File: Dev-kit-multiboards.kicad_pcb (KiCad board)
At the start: 2 copper layers, 93.9 x 100 mm, 27 parts, among them J1 Conn_01x04_Socket, J2 Conn_01x04_Socket, J3 Conn_01x02_Socket, J4 Conn_01x19_Socket, J5 Conn_01x19_Socket, J6 Conn_01x02_Socket, J7 Conn_01x02_Socket, J8 Conn_02x17_Counter_Clockwise

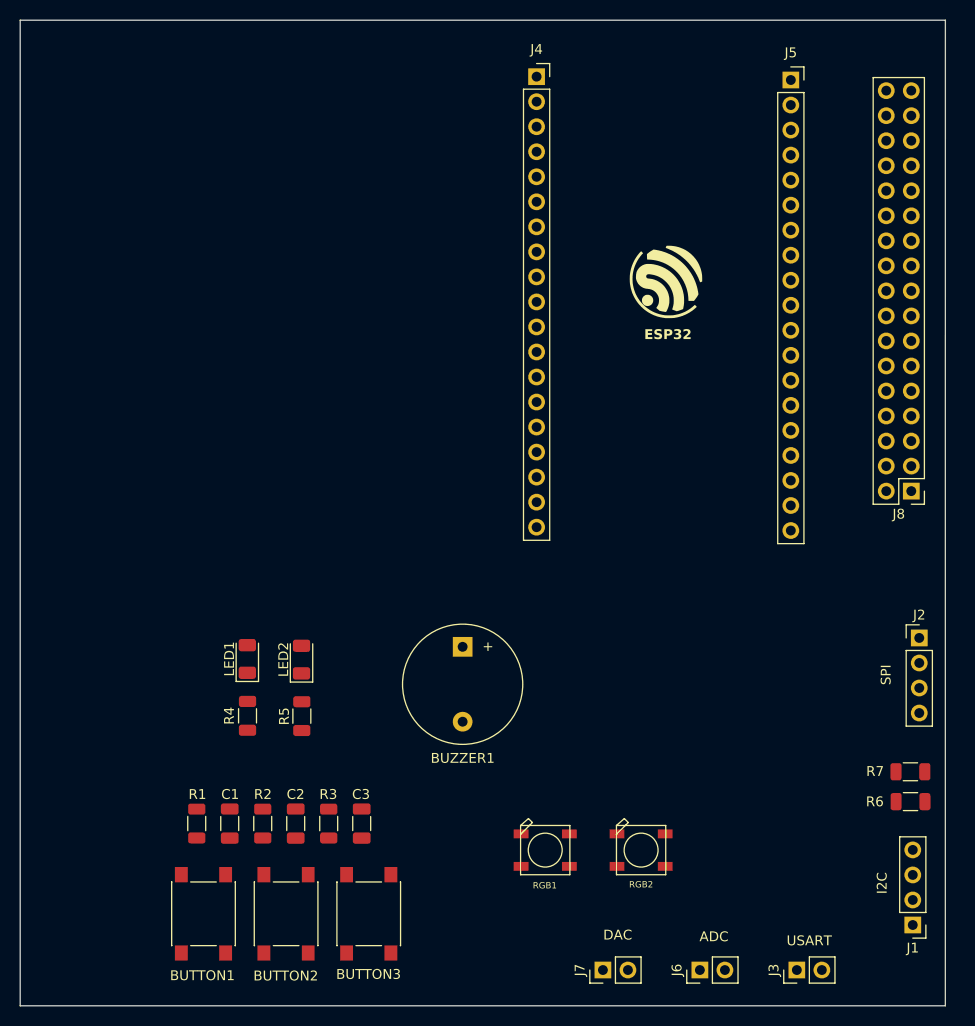
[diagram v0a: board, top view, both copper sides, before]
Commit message: Component placement ESP32
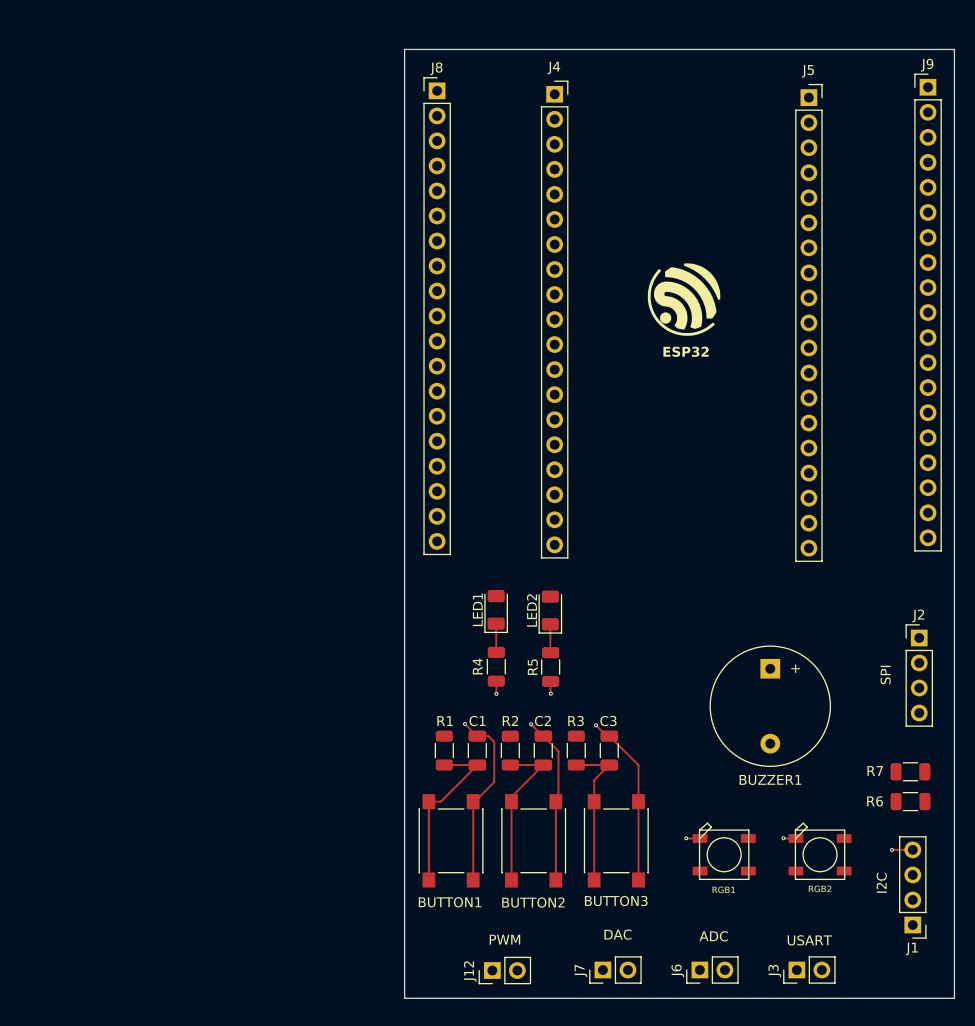
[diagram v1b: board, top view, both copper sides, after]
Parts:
- added J12: Conn_01x02_Socket, Connector_PinHeader_2.54mm:PinHeader_1x02_P2.54mm_Vertical, F.Cu at (99.4, 127.5)
- added J9: Conn_01x19, Connector_PinHeader_2.54mm:PinHeader_1x19_P2.54mm_Vertical, F.Cu at (143.7, 37.9)
- J8: value Conn_02x17_Counter_Clockwise -> Conn_01x19; footprint Connector_PinHeader_2.54mm:PinHeader_2x17_P2.54mm_Vertical -> Connector_PinHeader_2.54mm:PinHeader_1x19_P2.54mm_Vertical
- moved J8 63.0 mm to (93.8, 38.3), turned to 0 degrees
- moved BUZZER1 31.3 mm to (127.6, 96.9)
- moved BUTTON1 26.2 mm to (95.2, 114.4)
- moved BUTTON2 26.2 mm to (103.6, 114.4)
- moved BUTTON3 26.2 mm to (112.0, 114.4)
- moved C1 26.2 mm to (97.9, 105.2)
- moved C2 26.2 mm to (104.6, 105.2)
- moved C3 26.2 mm to (111.3, 105.2)
- moved R1 26.2 mm to (94.6, 105.2)
- moved R2 26.2 mm to (101.3, 105.2)
- moved R3 26.2 mm to (108.0, 105.2)
- moved LED1 25.7 mm to (99.8, 90.9)
- moved LED2 25.7 mm to (105.3, 91.0)
- moved R4 25.7 mm to (99.8, 96.7)
- moved R5 25.7 mm to (105.3, 96.7)
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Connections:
- J4 pad 3: ADC1_0 -> ADC1
- J5 pad 13: ADC2_0 -> ADC2
- J6 pad 1: ADC1_0 -> ADC1
- J6 pad 2: ADC2_0 -> ADC2
- J8 pad 1: IO0 -> +3.3V
- J8 pad 10: IO9 -> DAC_2
- J8 pad 11: IO10 -> IO27
- J8 pad 12: IO11 -> IO14
- J8 pad 14: IO13 -> Earth
- J8 pad 15: IO14 -> IO13
- J8 pad 16: BUTTON1 -> IO9
- J8 pad 17: IO39 -> IO10
- J8 pad 18: ADC1_0 -> IO11
- J8 pad 19: IO35 -> +5V
- J8 pad 2: IO1 -> EN_ESP32
- J8 pad 3: Buzzer -> ADC1
- J8 pad 4: IO3 -> IO39
- J8 pad 5: ADC2_0 -> IO34
- J8 pad 6: CS -> IO35
- J8 pad 7: IO6 -> IO32
- J8 pad 8: BUTTON3 -> IO33
- J8 pad 9: BUTTON2 -> DAC_1
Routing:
- net Earth: track 0.00 -> 60.7 mm, vias 0 -> 8
- net BUTTON1: track 0.00 -> 17.8 mm
- net BUTTON2: track 0.00 -> 16.3 mm
- net BUTTON3: track 0.00 -> 15.6 mm
- net Net-(LED1-K): track 0.00 -> 2.92 mm
- net Net-(LED2-K): track 0.00 -> 2.89 mm
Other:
- board size 93.9 x 100 mm -> 55.8 x 96.3 mm
- board text added: "PWM"

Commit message: Final version
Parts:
- removed R6, R7: 10K, Resistor_SMD:R_1206_3216Metric
- added J10: USB_B_Micro, Connector_USB:USB_Micro-B_Molex-105017-0001, F.Cu at (118.4, 126.2)
- added JP1: Jumper_2_Bridged, Connector_PinHeader_2.54mm:PinHeader_1x02_P2.54mm_Vertical, F.Cu at (125.8, 92.1)
- moved RGB1 9.73 mm to (132.7, 115.8)
- moved RGB2 9.73 mm to (123.0, 115.8)
- moved J3 9.28 mm to (139.6, 127.0)
- moved J6 8.45 mm to (128.9, 127.0)
- moved J1 5.97 mm to (142.6, 117.0)
- moved C1 3.35 mm to (94.6, 105.2)
- moved C2 3.35 mm to (101.3, 105.2)
- moved C3 3.35 mm to (108.0, 105.2)
- moved R1 3.35 mm to (97.9, 105.2)
- moved R2 3.35 mm to (104.6, 105.2)
- moved R3 3.35 mm to (111.3, 105.2)
- moved BUZZER1 2.92 mm to (130.0, 98.7)
- moved J7 2.63 mm to (108.1, 127.0), turned to -90 degrees
- moved J12 2.32 mm to (97.2, 127.0), turned to -90 degrees
- moved J9 0.36 mm to (143.7, 38.3)
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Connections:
- BUZZER1 pad 1: Buzzer -> Net-(BUZZER1--)
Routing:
- net ADC1: track 0.00 -> 105.6 mm, vias 0 -> 2
- net DAC_1: track 0.00 -> 89.8 mm, vias 0 -> 2
- net DAC_2: track 0.00 -> 88.5 mm, vias 0 -> 2
- net IO22: track 0.00 -> 86.8 mm
- net IO17: track 0.00 -> 84.1 mm, vias 0 -> 1
- net IO21: track 0.00 -> 83.6 mm
- net IO16: track 0.00 -> 80.5 mm, vias 0 -> 1
- net ADC2: track 0.00 -> 79.8 mm, vias 0 -> 3
- net IO10: track 0.00 -> 78.7 mm
- net IO11: track 0.00 -> 77.9 mm
- net IO27: track 0.00 -> 75.5 mm
- net IO12: track 0.00 -> 67.9 mm
- net IO23: track 0.00 -> 67.2 mm
- net +5V: track 0.00 -> 63.3 mm, vias 0 -> 1
- net CLK: track 0.00 -> 60.6 mm, vias 0 -> 1
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- added copper zone on F.Cu, net +3.3V
- added copper zone on B.Cu, net Earth
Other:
- board text added: "3V3"
- board text added: "5V"
- board text added: "ADC1"
- board text added: "ADC2"
- board text added: "CLK"
- board text added: "CS"
- board text added: "DAC1"
- board text added: "DAC2"
- board text added: "EN"
- board text added: "GND"
- board text added: "IO0"
- board text added: "IO1"
- board text added: "IO10"
- board text added: "IO11"
- board text added: "IO12"
- board text added: "IO13"
- board text added: "IO14"
- board text added: "IO15"
- board text added: "IO16"
- board text added: "IO17"
- board text added: "IO18"
- board text added: "IO19"
- board text added: "IO2"
- board text added: "IO21"
- board text added: "IO22"
- board text added: "IO23"
- board text added: "IO25"
- board text added: "IO26"
- board text added: "IO27"
- board text added: "IO3"
- board text added: "IO32"
- board text added: "IO33"
- board text added: "IO34"
- board text added: "IO35"
- board text added: "IO36"
- board text added: "IO39"
- board text added: "IO4"
- board text added: "IO5"
- board text added: "IO6"
- board text added: "IO7"
- board text added: "IO8"
- board text added: "IO9"
- board text added: "MISO"
- board text added: "MOSI"
- board text added: "PWM1"
- board text added: "PWM2"
- board text added: "RX"
- board text added: "SCL"
- board text added: "SDA"
- board text added: "TX"
